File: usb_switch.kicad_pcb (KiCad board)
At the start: 2 copper layers, 55 x 43 mm, 59 parts, among them CON1 USB, CON2 2_Post_Terminal, CON3 2_Post_Terminal, CON4 2_Post_Terminal, CON5 2_Post_Terminal, CON6 2_Post_Terminal, CON7 2_Post_Terminal, U1 AP2120N, U2 STM32F042K6T6, U3 Si1869DH, U4 Si1869DH, U5 Si1869DH, U6 Si1869DH, U7 Si1869DH

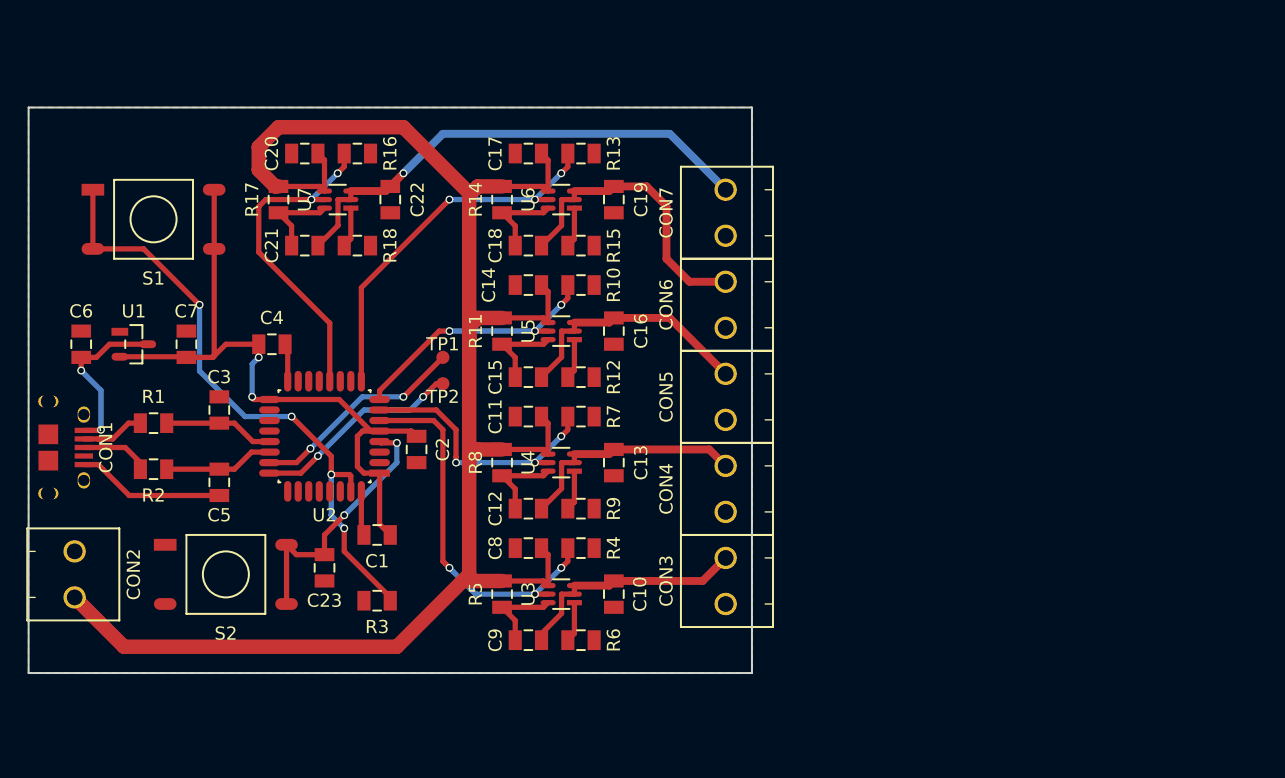
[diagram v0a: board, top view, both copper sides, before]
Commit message: More hacking on the PCB layout, also adding a fuse component.
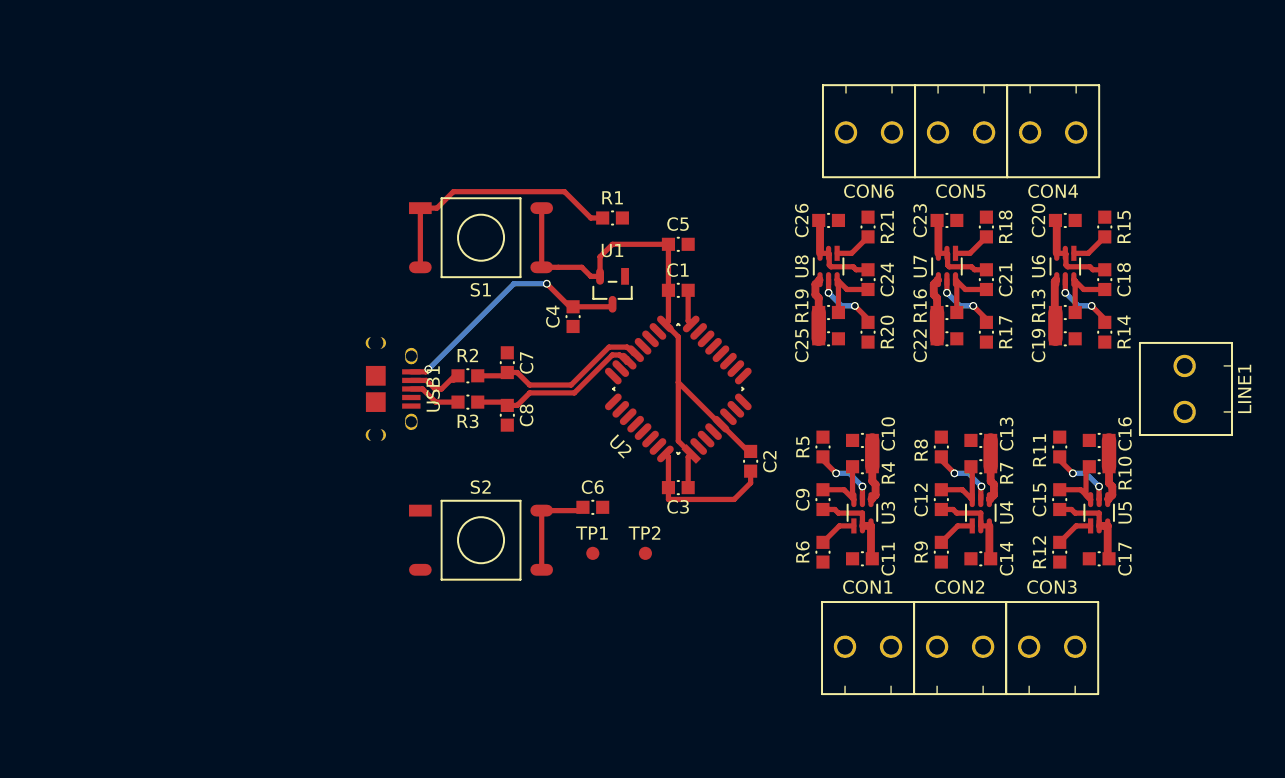
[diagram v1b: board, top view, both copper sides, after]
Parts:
- removed CON7: 2_Post_Terminal, parts:2_Post_Terminal_OSTTE020104
- added C24: 1µF, parts:Capacitor_0603, F.Cu at (138.8, 81.1)
- added C25: 10µF, parts:Capacitor_0603, F.Cu at (135.8, 85.6)
- added C26: 1µF, parts:Capacitor_0603, F.Cu at (135.8, 76.6)
- added LINE1: 2_Post_Terminal, parts:2_Post_Terminal_OSTTE020104, F.Cu at (162.9, 89.4)
- added R19: 10k, parts:Resistor_0603, F.Cu at (135.8, 83.6)
- added R20: 10k, parts:Resistor_0603, F.Cu at (138.8, 85.1)
- added R21: 2k, parts:Resistor_0603, F.Cu at (138.8, 77.1)
- added U8: Si1869DH, parts:Si1869DH_SC70-6, F.Cu at (135.8, 80.1)
- added USB1: USB, parts:USB_Micro_SMD_RA, F.Cu at (101.4, 89.4)
- C1, C12, C15, C18, C2, C21, C9: footprint parts:Capacitor_0805 -> parts:Capacitor_0603
- C10, C13, C16, C19, C22: value 1µF -> 10µF; footprint parts:Capacitor_0805 -> parts:Capacitor_0603
- C11, C14, C17, C20: value 10µF -> 1µF; footprint parts:Capacitor_0805 -> parts:Capacitor_0603
- C23, C4: value 100nF -> 1µF; footprint parts:Capacitor_0805 -> parts:Capacitor_0603
- C3: value 47pF -> 100nF; footprint parts:Capacitor_0805 -> parts:Capacitor_0603
- C5: value 47pF -> 10µF; footprint parts:Capacitor_0805 -> parts:Capacitor_0603
- C6: value 1µF -> 100nF; footprint parts:Capacitor_0805 -> parts:Capacitor_0603
- C7, C8: value 10µF -> 47pF; footprint parts:Capacitor_0805 -> parts:Capacitor_0603
- CON1: value USB -> 2_Post_Terminal; footprint parts:USB_Micro_SMD_RA -> parts:2_Post_Terminal_OSTTE020104
- R1: value 22R -> 10k; footprint parts:Resistor_0805 -> parts:Resistor_0603
- R10, R11, R12, R13, R14, R15, R16, R17, R18, R2, R4, R5, R6, R7, R8, R9: footprint parts:Resistor_0805 -> parts:Resistor_0603
- R3: value 10k -> 22R; footprint parts:Resistor_0805 -> parts:Resistor_0603
- moved CON2 67.6 mm to (145.8, 109.0), turned to 180 degrees
- moved CON1 64.1 mm to (138.8, 109.0), turned to 180 degrees
- moved C20 58.0 mm to (153.8, 76.6)
- moved R17 54.8 mm to (147.8, 85.1), turned to 90 degrees
- moved C23 54.2 mm to (144.8, 76.6), turned to 0 degrees
- moved C17 53.2 mm to (156.4, 102.3), turned to 180 degrees
- moved C21 51.9 mm to (147.8, 81.1), turned to 270 degrees
- moved R18 47.8 mm to (147.8, 77.1), turned to 270 degrees
- moved R14 46.9 mm to (156.8, 85.1), turned to 90 degrees
- moved U7 46.6 mm to (144.8, 80.1), turned to 270 degrees
- moved R16 46.4 mm to (144.8, 83.6), turned to 0 degrees
- moved C18 43.9 mm to (156.8, 81.1), turned to 270 degrees
- moved C22 43.6 mm to (144.8, 85.6), turned to 180 degrees
- moved R11 43.3 mm to (153.4, 93.8)
- moved U5 43.2 mm to (156.4, 98.8), turned to 90 degrees
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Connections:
- C10 pad 1: Net-(C10-Pad1) -> GND
- C10 pad 2: GND -> Line
- C11 pad 1: GND -> Net-(C11-Pad1)
- C11 pad 2: Line -> GND
- C13 pad 1: Net-(C12-Pad1) -> GND
- C13 pad 2: GND -> Line
- C14 pad 1: GND -> Net-(C12-Pad1)
- C14 pad 2: Line -> GND
- C16 pad 1: Net-(C15-Pad1) -> GND
- C16 pad 2: GND -> Line
- C17 pad 1: GND -> Net-(C15-Pad1)
- C17 pad 2: Line -> GND
- C19 pad 1: Net-(C18-Pad1) -> GND
- C19 pad 2: GND -> Line
- C20 pad 1: GND -> Net-(C18-Pad1)
- C20 pad 2: Line -> GND
- C22 pad 1: Net-(C21-Pad1) -> GND
- C22 pad 2: GND -> Line
- C23 pad 1: Net-(C23-Pad1) -> Net-(C21-Pad1)
- C3 pad 2: /USB_D+ -> +3.3V
- C4 pad 2: +3.3V -> +5V
- C5 pad 2: /USB_D- -> +3.3V
- C6 pad 1: GND -> Net-(C6-Pad1)
- C6 pad 2: +5V -> GND
- C7 pad 2: +3.3V -> /USB_D+
- C8 pad 2: Line -> /USB_D-
- C9 pad 1: Net-(C10-Pad1) -> Net-(C11-Pad1)
- CON1 pad 1: +5V -> Net-(C11-Pad1)
- CON1 pad 2: /D+ -> GND
- CON2 pad 1: Line -> Net-(C12-Pad1)
- CON3 pad 1: Net-(C10-Pad1) -> Net-(C15-Pad1)
- CON4 pad 1: Net-(C12-Pad1) -> Net-(C18-Pad1)
- CON5 pad 1: Net-(C15-Pad1) -> Net-(C21-Pad1)
- CON6 pad 1: Net-(C18-Pad1) -> Net-(C24-Pad1)
- R1 pad 1: /D+ -> GND
- R1 pad 2: /USB_D+ -> Net-(R1-Pad2)
- R10 pad 1: GND -> Line
- R10 pad 2: /Switch 3/SW -> Net-(C15-Pad2)
- R11 pad 1: Line -> GND
- R11 pad 2: Net-(C15-Pad2) -> /Switch 3/SW
- R13 pad 1: GND -> Line
- R13 pad 2: /Switch 4/SW -> Net-(C18-Pad2)
- R14 pad 1: Line -> GND
- R14 pad 2: Net-(C18-Pad2) -> /Switch 4/SW
- R16 pad 1: GND -> Line
- R16 pad 2: /Switch 5/SW -> Net-(C21-Pad2)
- R17 pad 1: Line -> GND
- R17 pad 2: Net-(C21-Pad2) -> /Switch 5/SW
- R2 pad 1: /D- -> /D+
- R2 pad 2: /USB_D- -> /USB_D+
- R3 pad 1: GND -> /D-
- R3 pad 2: Net-(R3-Pad2) -> /USB_D-
- R4 pad 1: GND -> Line
- R4 pad 2: /Switch 1/SW -> Net-(C9-Pad2)
- R5 pad 1: Line -> GND
- R5 pad 2: Net-(C9-Pad2) -> /Switch 1/SW
- R7 pad 1: GND -> Line
- R7 pad 2: /Switch 2/SW -> Net-(C12-Pad2)
- R8 pad 1: Line -> GND
- R8 pad 2: Net-(C12-Pad2) -> /Switch 2/SW
- S1 pad 1: Net-(R3-Pad2) -> Net-(R1-Pad2)
- S1 pad 2: Net-(R3-Pad2) -> Net-(R1-Pad2)
- S2 pad 3: Net-(C23-Pad1) -> Net-(C6-Pad1)
- S2 pad 4: Net-(C23-Pad1) -> Net-(C6-Pad1)
- U2 pad 10: Net-(U2-Pad10) -> (no net)
- U2 pad 11: Net-(U2-Pad11) -> (no net)
- U2 pad 13: Net-(U2-Pad13) -> /Switch 6/SW
- U2 pad 14: Net-(U2-Pad14) -> (no net)
- U2 pad 15: Net-(U2-Pad15) -> (no net)
- U2 pad 18: Net-(U2-Pad18) -> (no net)
- U2 pad 19: Net-(U2-Pad19) -> (no net)
- U2 pad 2: Net-(U2-Pad2) -> (no net)
- U2 pad 20: Net-(U2-Pad20) -> (no net)
- U2 pad 25: Net-(U2-Pad25) -> (no net)
- U2 pad 26: Net-(U2-Pad26) -> (no net)
- U2 pad 27: Net-(U2-Pad27) -> (no net)
- U2 pad 28: Net-(U2-Pad28) -> (no net)
- U2 pad 29: Net-(U2-Pad29) -> (no net)
- U2 pad 3: Net-(U2-Pad3) -> (no net)
- U2 pad 30: Net-(U2-Pad30) -> (no net)
- U2 pad 31: Net-(R3-Pad2) -> Net-(R1-Pad2)
- U2 pad 4: Net-(C23-Pad1) -> Net-(C6-Pad1)
- U3 pad 2: Net-(C10-Pad1) -> Net-(C11-Pad1)
- U3 pad 3: Net-(C10-Pad1) -> Net-(C11-Pad1)
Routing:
- net Line: track 131.5 -> 28.2 mm
- net Net-(R3-Pad2): track 47.7 -> 0.00 mm, vias 4 -> 0
- net Net-(C21-Pad1): track 37.8 -> 7.20 mm, vias 1 -> 0
- net /Switch 1/SW: track 28.7 -> 5.08 mm, vias 3 -> 2
- net /Switch 4/SW: track 28.6 -> 5.08 mm, vias 3 -> 2
- net /Switch 5/SW: track 25.3 -> 5.08 mm
- net Net-(C23-Pad1): track 19.8 -> 0.00 mm, vias 2 -> 0
- net Net-(R1-Pad2): track 0.00 -> 19.7 mm
- net Net-(C10-Pad1): track 18.1 -> 0.00 mm
- net Net-(TP1-Pad1): track 16.5 -> 0.00 mm, vias 2 -> 0
- net Net-(TP2-Pad1): track 16.0 -> 0.00 mm, vias 2 -> 0
- net Net-(C18-Pad1): track 22.7 -> 7.20 mm
- net /Switch 2/SW: track 20.5 -> 5.15 mm, vias 3 -> 2
- net /Switch 3/SW: track 19.9 -> 5.07 mm, vias 3 -> 2
- net Net-(C15-Pad1): track 19.2 -> 7.23 mm
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- removed copper zone on B.Cu, net GND
- removed copper zone on F.Cu, net GND
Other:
- board outline removed

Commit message: Finish routing the PCB.
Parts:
- added F1: 2A, parts:Fuse_Block, F.Cu at (145.9, 89.4)
- moved S1 28.6 mm to (126.4, 100.9)
- moved C7 26.5 mm to (125.4, 64.9)
- moved C8 26.5 mm to (125.4, 68.9)
- moved R2 26.5 mm to (122.4, 65.9)
- moved R3 26.5 mm to (122.4, 67.9)
- moved USB1 26.5 mm to (115.4, 66.9)
- moved R1 24.5 mm to (118.4, 100.9), turned to 270 degrees
- moved S2 19.2 mm to (126.4, 109.9), turned to 180 degrees
- moved C4 18.8 mm to (130.4, 71.4), turned to 0 degrees
- moved U1 13.0 mm to (130.4, 74.9), turned to 0 degrees
- moved C6 11.5 mm to (118.4, 109.9), turned to 270 degrees
- moved TP2 8.06 mm to (117.9, 94.9)
- moved TP1 7.16 mm to (116.4, 94.9)
- moved C10 4.00 mm to (138.4, 97.3)
- moved C11 4.00 mm to (138.4, 106.3)
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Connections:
- LINE1 pad 1: Line -> Net-(F1-Pad1)
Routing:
- net GND: track 13.9 -> 127.2 mm
- net Line: track 28.2 -> 100.8 mm
- net /Switch 3/SW: track 5.07 -> 35.1 mm, vias 2 -> 3
- net /Switch 4/SW: track 5.08 -> 34.1 mm, vias 2 -> 3
- net Net-(C6-Pad1): track 7.74 -> 29.4 mm
- net /Switch 2/SW: track 5.15 -> 26.5 mm, vias 2 -> 3
- net /Switch 5/SW: track 5.08 -> 25.0 mm, vias 2 -> 3
- net /Switch 1/SW: track 5.08 -> 20.3 mm, vias 2 -> 3
- net /USB_D-: track 13.7 -> 26.6 mm, vias 0 -> 2
- net Net-(TP1-Pad1): track 0.00 -> 12.7 mm
- net /USB_D+: track 14.2 -> 26.6 mm, vias 0 -> 2
- net /Switch 6/SW: track 5.08 -> 16.1 mm, vias 2 -> 3
- net Net-(F1-Pad1): track 0.00 -> 10.2 mm
- net Net-(TP2-Pad1): track 0.00 -> 9.63 mm
- net +3.3V: track 43.5 -> 51.6 mm
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- added copper zone on B.Cu, net GND
- added copper zone on F.Cu, net GND
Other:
- board outline added: 52.5 x 55 mm

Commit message: Sent to fab.
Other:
- board text added: "CON1-6: 1A max each"
- board text added: "LINE1: 18V/2A max"
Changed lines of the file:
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@@
     (links 143)
     (no_connects 0)
-    (area 0 0 0 0)
+    (area 111.125 61.624999 166.775001 116.975001)
     (thickness 1.6)
-    (drawings 5)
+    (drawings 7)
     (tracks 428)
     (zones 0)
@@
     (uvia_drill 0.1)
     (add_net Line)
+  )
+  (module parts:USB_Micro_SMD_RA (layer F.Cu)
+    (at 115.4 66.9 270)
+    (descr "Micro B right angle SMD")
+    (fp_text reference USB1 (at 0 -4.4 270) (layer F.SilkS)
+      (effects (font (size 1 1) (thickness 0.15)))
+    )
+    (fp_text value USB (at 0 3.15 270) (layer F.Fab)
+      (effects (font (size 1 1) (thickness 0.15)))
+    )
+    (fp_line (start -5 1.45) (end 5 1.45) (layer F.Fab) (width 0.15))
+    (fp_line (start -4 2.15) (end 4 2.15) (layer F.Fab) (width 0.15))
+    (fp_line (start 4 2.15) (end 4 -2.85) (layer F.Fab) (width 0.15))
+    (fp_line (start 4 -2.85) (end -4 -2.85) (layer F.Fab) (width 0.15))
+    (fp_line (start -4 -2.85) (end -4 2.15) (layer F.Fab) (width 0.15))
+    (pad 1 smd rect (at -1.3 -2.7 270) (size 0.4 1.4) (layers F.Cu F.Paste F.Mask)
+      (net 3 +5V))
+    (pad 2 smd rect (at -0.65 -2.7 270) (size 0.4 1.4) (layers F.Cu F.Paste F.Mask)
+      (net 12 /D+))
+    (pad 3 smd rect (at 0 -2.7 270) (size 0.4 1.4) (layers F.Cu F.Paste F.Mask)
+      (net 13 /D-))
+    (pad 4 smd rect (at 0.65 -2.7 270) (size 0.4 1.4) (layers F.Cu F.Paste F.Mask))
+    (pad 5 smd rect (at 1.3 -2.7 270) (size 0.4 1.4) (layers F.Cu F.Paste F.Mask)
+      (net 1 GND))
+    (pad shel thru_hole oval (at -2.5 -2.7 270) (size 1.25 0.95) (drill oval 0.85 0.55) (layers *.Cu *.Mask F.SilkS))
+    (pad shel thru_hole oval (at 2.5 -2.7 270) (size 1.25 0.95) (drill oval 0.85 0.55) (layers *.Cu *.Mask F.SilkS))
+    (pad shel thru_hole oval (at -3.5 0 270) (size 0.9 1.55) (drill oval 0.5 1.15) (layers *.Cu *.Mask F.SilkS))
+    (pad shel thru_hole oval (at 3.5 0 270) (size 0.9 1.55) (drill oval 0.5 1.15) (layers *.Cu *.Mask F.SilkS))
+    (pad shel smd rect (at -1 0 270) (size 1.5 1.5) (layers F.Cu F.Paste F.Mask))
+    (pad shel smd rect (at 1 0 270) (size 1.5 1.5) (layers F.Cu F.Paste F.Mask))
   )
   (module parts:STM32F042K6T6_32-QFP (layer F.Cu)
@@
       (net 11 /USB_D-))
   )
-  (module parts:USB_Micro_SMD_RA (layer F.Cu)
-    (at 115.4 66.9 270)
-    (descr "Micro B right angle SMD")
-    (fp_text reference USB1 (at 0 -4.4 270) (layer F.SilkS)
-      (effects (font (size 1 1) (thickness 0.15)))
-    )
-    (fp_text value USB (at 0 3.15 270) (layer F.Fab)
-      (effects (font (size 1 1) (thickness 0.15)))
-    )
-    (fp_line (start -5 1.45) (end 5 1.45) (layer F.Fab) (width 0.15))
-    (fp_line (start -4 2.15) (end 4 2.15) (layer F.Fab) (width 0.15))
-    (fp_line (start 4 2.15) (end 4 -2.85) (layer F.Fab) (width 0.15))
-    (fp_line (start 4 -2.85) (end -4 -2.85) (layer F.Fab) (width 0.15))
-    (fp_line (start -4 -2.85) (end -4 2.15) (layer F.Fab) (width 0.15))
-    (pad 1 smd rect (at -1.3 -2.7 270) (size 0.4 1.4) (layers F.Cu F.Paste F.Mask)
-      (net 3 +5V))
-    (pad 2 smd rect (at -0.65 -2.7 270) (size 0.4 1.4) (layers F.Cu F.Paste F.Mask)
-      (net 12 /D+))
-    (pad 3 smd rect (at 0 -2.7 270) (size 0.4 1.4) (layers F.Cu F.Paste F.Mask)
-      (net 13 /D-))
-    (pad 4 smd rect (at 0.65 -2.7 270) (size 0.4 1.4) (layers F.Cu F.Paste F.Mask))
-    (pad 5 smd rect (at 1.3 -2.7 270) (size 0.4 1.4) (layers F.Cu F.Paste F.Mask)
-      (net 1 GND))
-    (pad shel thru_hole oval (at -2.5 -2.7 270) (size 1.25 0.95) (drill 0.85) (layers *.Cu *.Mask F.SilkS))
-    (pad shel thru_hole oval (at 2.5 -2.7 270) (size 1.25 0.95) (drill 0.85) (layers *.Cu *.Mask F.SilkS))
-    (pad shel thru_hole oval (at -3.5 0 270) (size 0.9 1.55) (drill 1.15) (layers *.Cu *.Mask F.SilkS))
-    (pad shel thru_hole oval (at 3.5 0 270) (size 0.9 1.55) (drill 1.15) (layers *.Cu *.Mask F.SilkS))
-    (pad shel smd rect (at -1 0 270) (size 1.5 1.5) (layers F.Cu F.Paste F.Mask))
-    (pad shel smd rect (at 1 0 270) (size 1.5 1.5) (layers F.Cu F.Paste F.Mask))
-  )
   (module parts:Resistor_0603 (layer F.Cu)
     (at 122.4 67.9)
@@
     (pad 3 thru_hole circle (at 0 0 180) (size 3 3) (drill 2.6) (layers *.Cu *.Mask F.SilkS))
   )
+  (gr_text "CON1-6:\n1A max each" (at 162.9 77.9 90) (layer F.SilkS)
+    (effects (font (size 1.5 1.5) (thickness 0.2)))
+  )
+  (gr_text "LINE1:\n18V/2A max" (at 162.9 100.9 90) (layer F.SilkS)
+    (effects (font (size 1.5 1.5) (thickness 0.2)))
+  )
   (gr_line (start 113.9 116.9) (end 113.9 61.9) (layer Edge.Cuts) (width 0.15))
   (gr_line (start 166.4 116.9) (end 113.9 116.9) (layer Edge.Cuts) (width 0.15))
   (gr_line (start 166.4 61.9) (end 166.4 116.9) (layer Edge.Cuts) (width 0.15))
   (gr_line (start 113.9 61.9) (end 166.4 61.9) (layer Edge.Cuts) (width 0.15))
-  (gr_text "(c) 2015 David Anderson <dave@natulte.net>\nLicense: Creative Commons Attribution 4.0 International\n" (at 53.34 152.4) (layer B.SilkS)
+  (gr_text "(c) 2015 David Anderson <dave@natulte.net>\nLicense: Creative Commons Attribution 4.0 International\n" (at 140.9 108.9) (layer B.SilkS)
     (effects (font (size 1 1) (thickness 0.2)) (justify mirror))
   )
